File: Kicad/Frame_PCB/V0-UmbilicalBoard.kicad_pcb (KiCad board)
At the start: 2 copper layers, 122 x 37 mm, 16 parts, among them J1 Conn_02x08_Odd_Even, J10 Neopixel Strip 1, J11 Neopixel Strip 1, J12 Neopixel Out, J2 Motor, J3 Hotend Fan, J4 Part Cooling Fan, J5 Heater, J6 Thermistor, J7 X-Endstop, J8 Chamber Thermistor, J9 Neopixel (from controller)

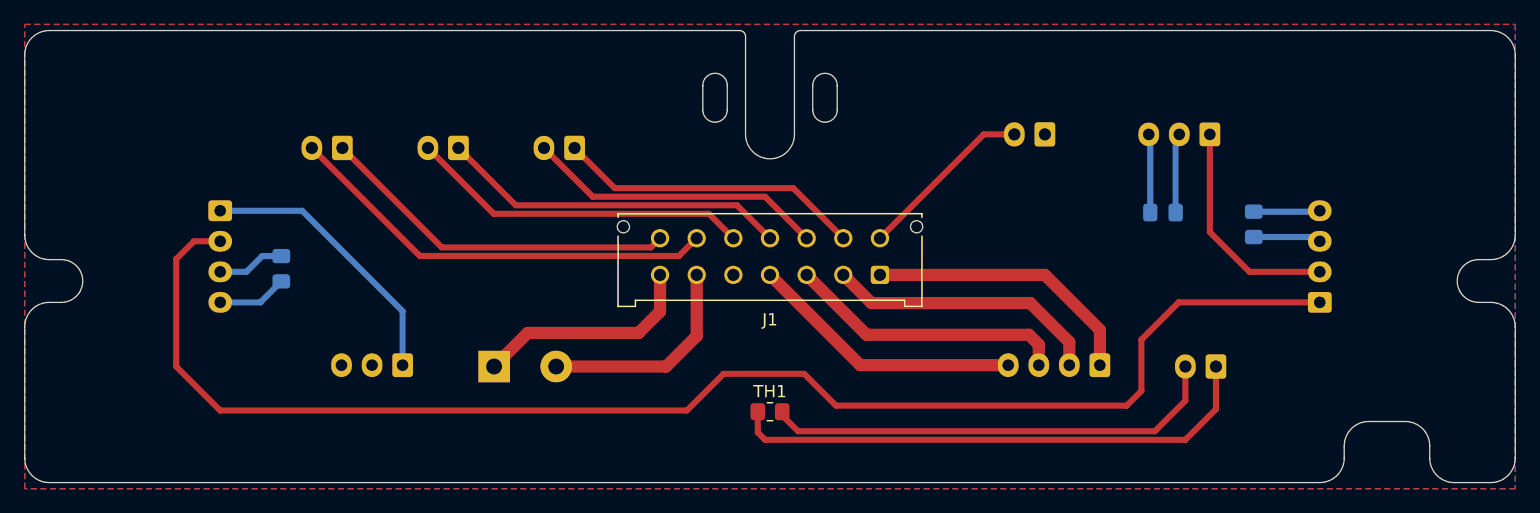
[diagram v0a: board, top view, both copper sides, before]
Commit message: Changed Micro Fit connector to 20 pin type and added 6-pin XH for accelerometer. Changed silkscreen text
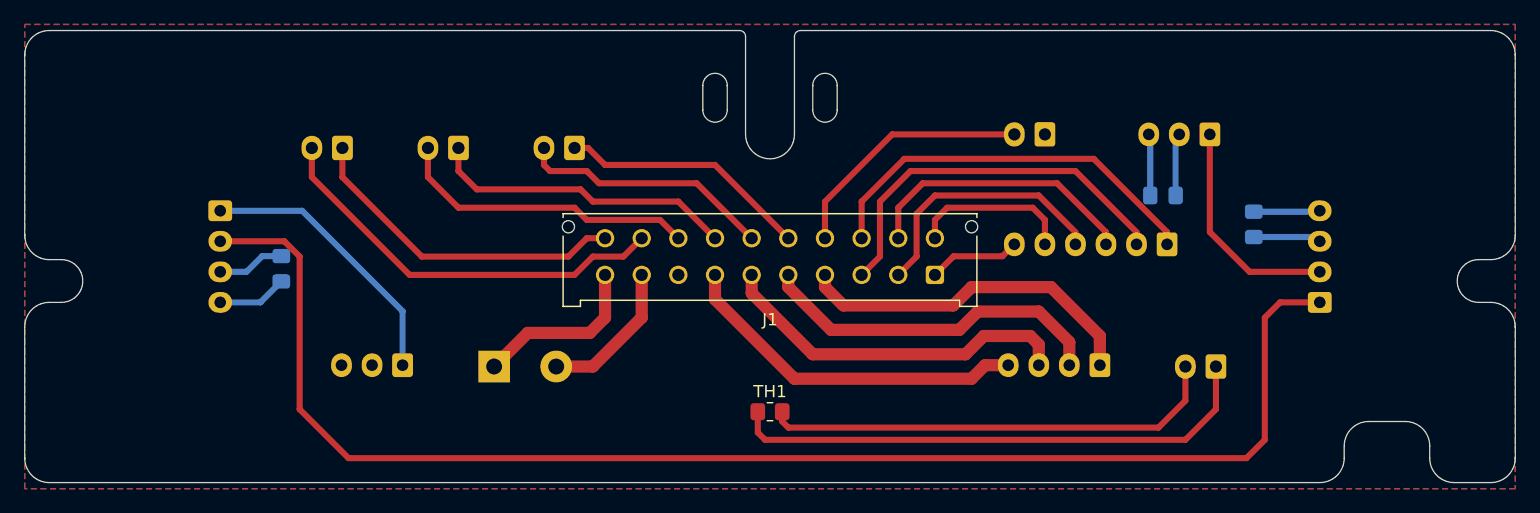
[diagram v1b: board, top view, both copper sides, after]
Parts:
- added J13: Accelerometer, Connector_JST:JST_XH_B6B-XH-A_1x06_P2.50mm_Vertical, B.Cu at (132.5, 99.0)
- J1: value Conn_02x08_Odd_Even -> Conn_02x10_Top_Bottom; footprint Connector_Molex:Molex_Micro-Fit_3.0_43045-1412_2x07_P3.00mm_Vertical -> Connector_Molex:Molex_Micro-Fit_3.0_43045-2012_2x10_P3.00mm_Vertical
- moved J1 4.50 mm to (113.5, 101.5)
- moved C2 1.40 mm to (132.2, 95.0)
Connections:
- J1 pad 1: /A1 -> /ADXL_GND
- J1 pad 10: /PartFan- -> Net-(J1-Pad10)
- J1 pad 11: /Hotend_Fan- -> /ADXL_SCLK
- J1 pad 12: /Hotend_Fan+ -> /ADXL_SDI
- J1 pad 13: Net-(J1-Pad13) -> /ADXL_VCC
- J1 pad 2: /A2 -> /ADXL_SDO
- J1 pad 3: /B1 -> /ADXL_CS
- J1 pad 4: /B2 -> /A1
- J1 pad 5: Ground -> /A2
- J1 pad 6: Net-(J1-Pad6) -> /B1
- J1 pad 7: Net-(J1-Pad7) -> /B2
- J1 pad 8: Net-(J1-Pad8) -> Ground
- J1 pad 9: /PartFan+ -> Net-(J1-Pad9)
- J5 pad 1: Net-(J1-Pad7) -> Net-(J1-Pad10)
- J5 pad 2: Net-(J1-Pad6) -> Net-(J1-Pad9)
- J6 pad 1: Net-(J1-Pad14) -> Net-(J1-Pad20)
- J6 pad 2: Net-(J1-Pad13) -> Net-(J1-Pad19)
- J7 pad 2: Net-(J1-Pad8) -> Net-(J1-Pad14)
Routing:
- net Net-(J1-Pad13): track 35.8 -> 0.00 mm
- net Net-(J1-Pad19): track 0.00 -> 33.9 mm
- net /ADXL_VCC: track 0.00 -> 32.9 mm
- net /ADXL_CS: track 0.00 -> 31.7 mm
- net Net-(J1-Pad20): track 0.00 -> 27.2 mm
- net /ADXL_SDI: track 0.00 -> 23.0 mm
- net /ADXL_SDO: track 0.00 -> 21.5 mm
- net Net-(J1-Pad7): track 18.4 -> 0.00 mm
- net Net-(J1-Pad6): track 17.5 -> 0.00 mm
- net Net-(J1-Pad8): track 14.5 -> 0.00 mm
- net Net-(J1-Pad10): track 0.00 -> 14.2 mm
- net /ADXL_SCLK: track 0.00 -> 13.3 mm
- net Net-(J1-Pad9): track 0.00 -> 12.2 mm
- net Net-(J1-Pad14): track 29.7 -> 20.8 mm
- net /ADXL_GND: track 0.00 -> 7.54 mm
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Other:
- net class Default removed
- board text added: "V0 Umbilical Breakout Board Plus Rev A - 1/25/22 S. Kueppers T. Abraham"
- board text added: "VCC CS SDI SDO SCK GND Accelerometer"
- board text removed: "V0 Umbilical Breakout Board Rev A - 4/20/21 T. Abraham"
